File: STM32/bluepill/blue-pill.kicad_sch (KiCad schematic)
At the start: 35 parts

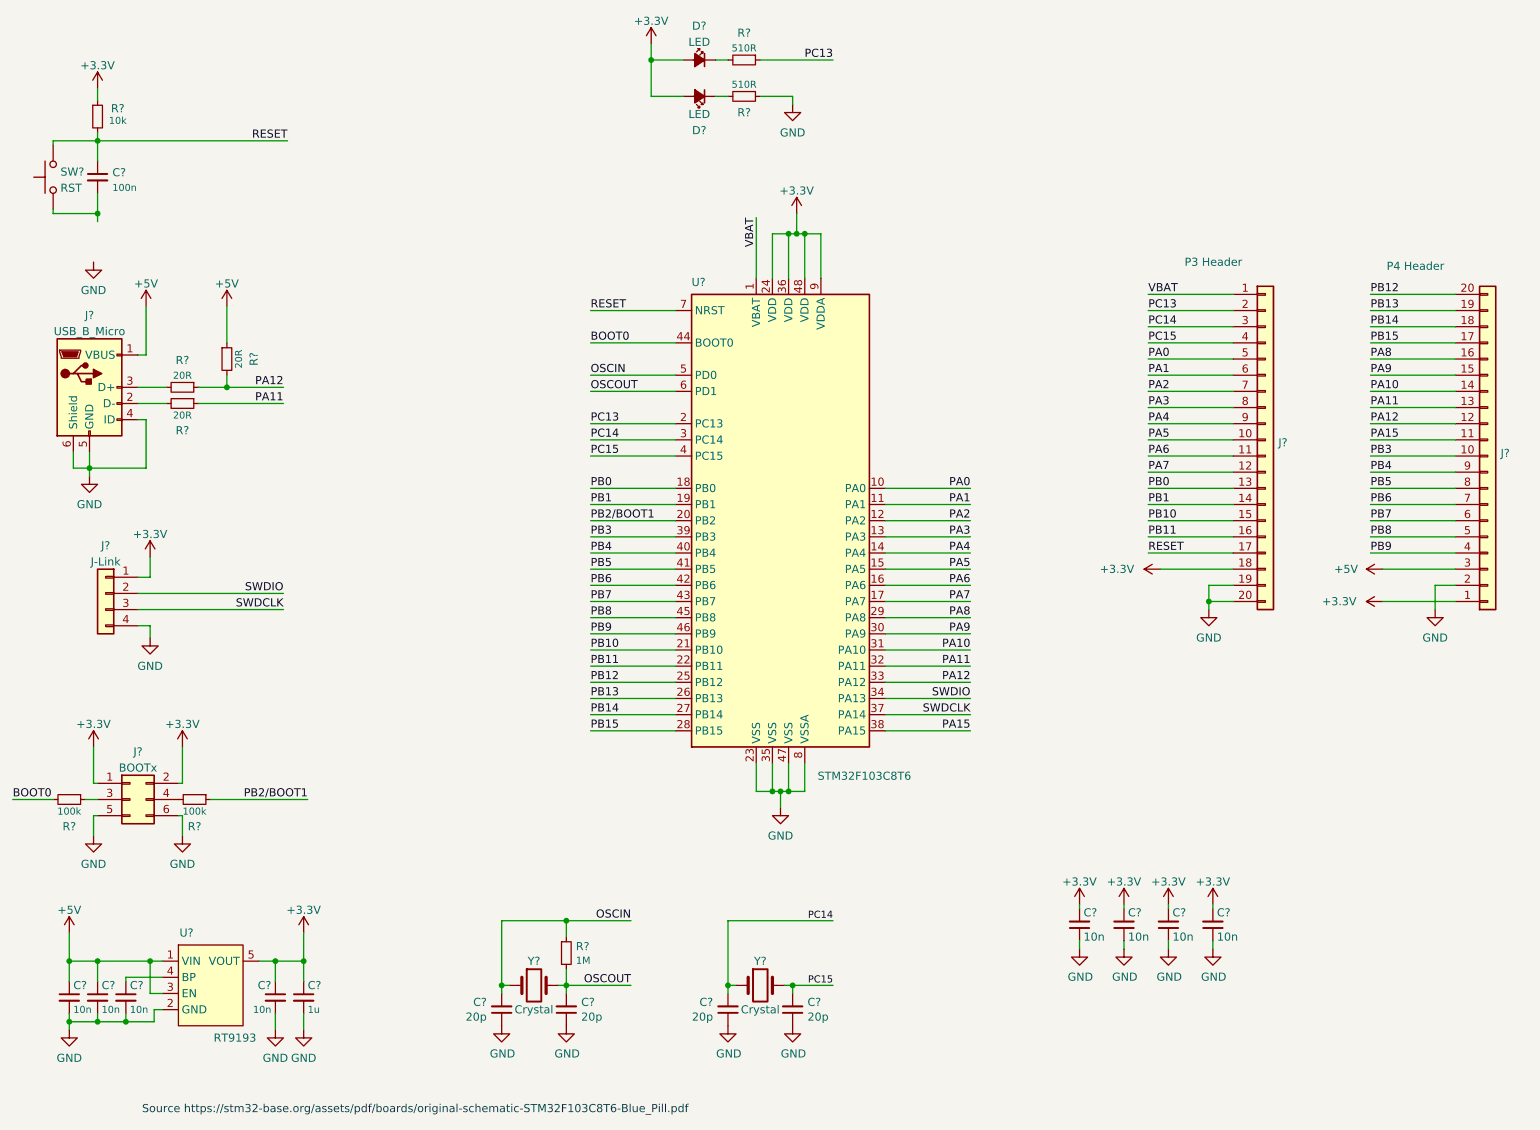
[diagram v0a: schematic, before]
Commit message: Fix ground on RST button
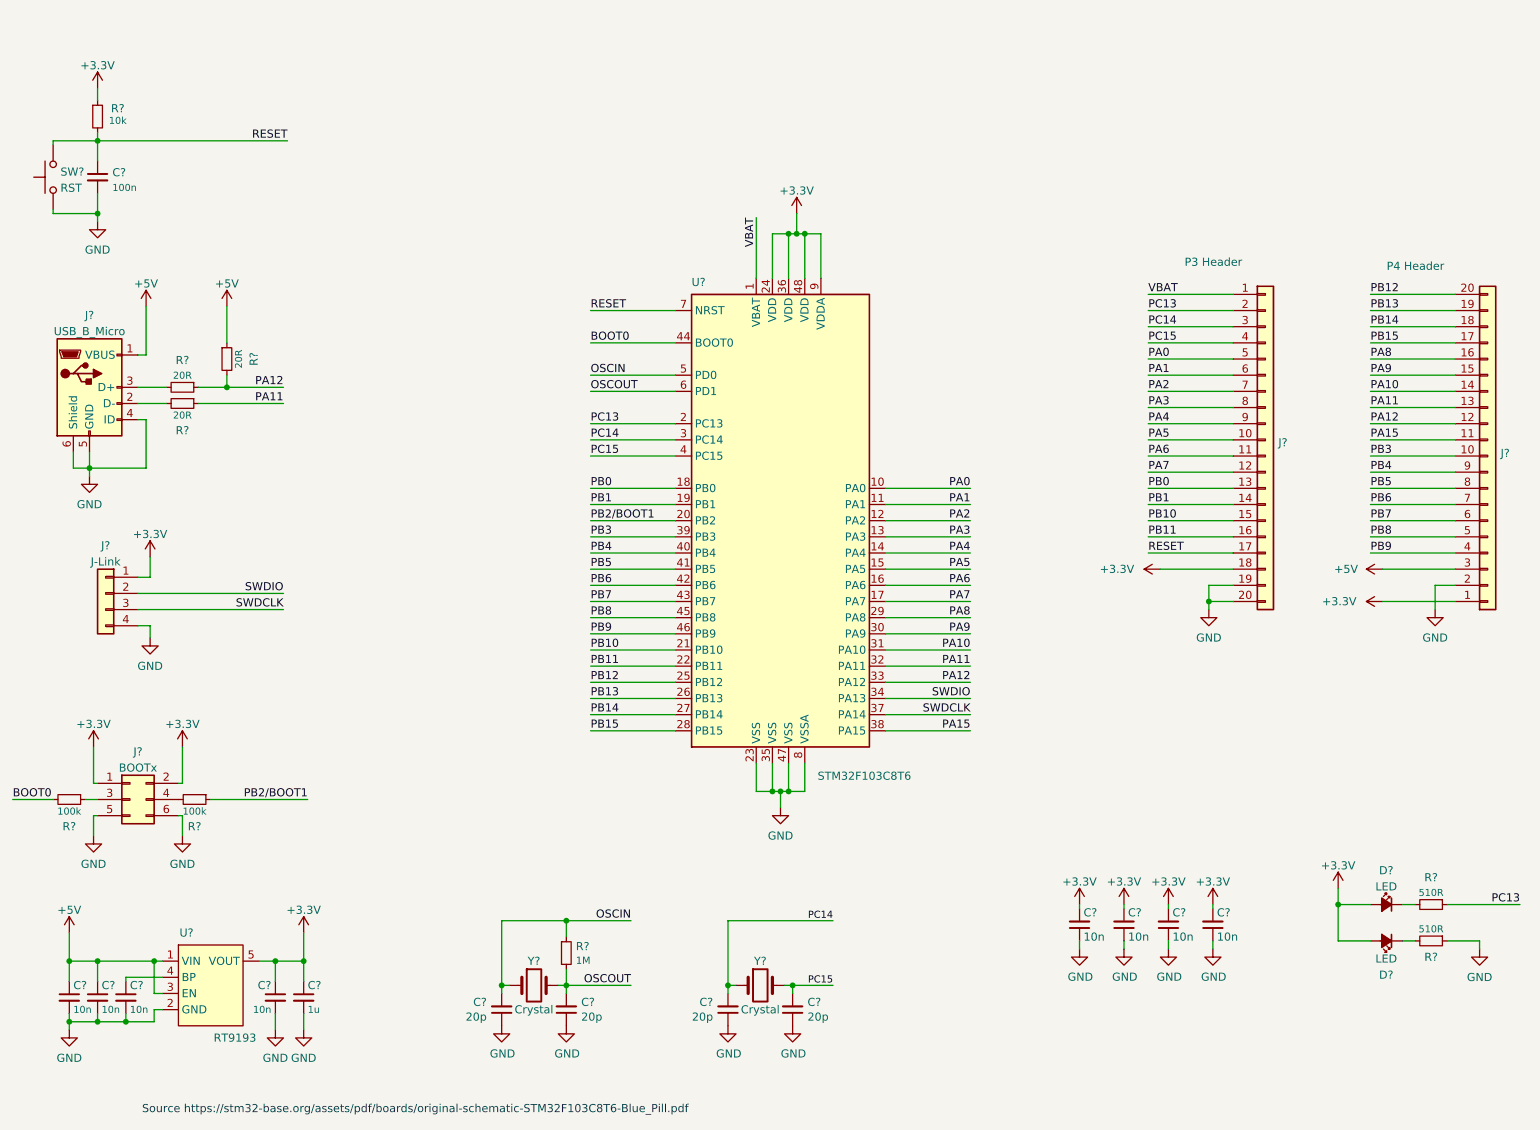
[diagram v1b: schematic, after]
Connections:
- net GND: now also C?.2, SW?.1
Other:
- moved on the sheet: D?, R?

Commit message: Fix input in RT919.3 Fix some resistors values.
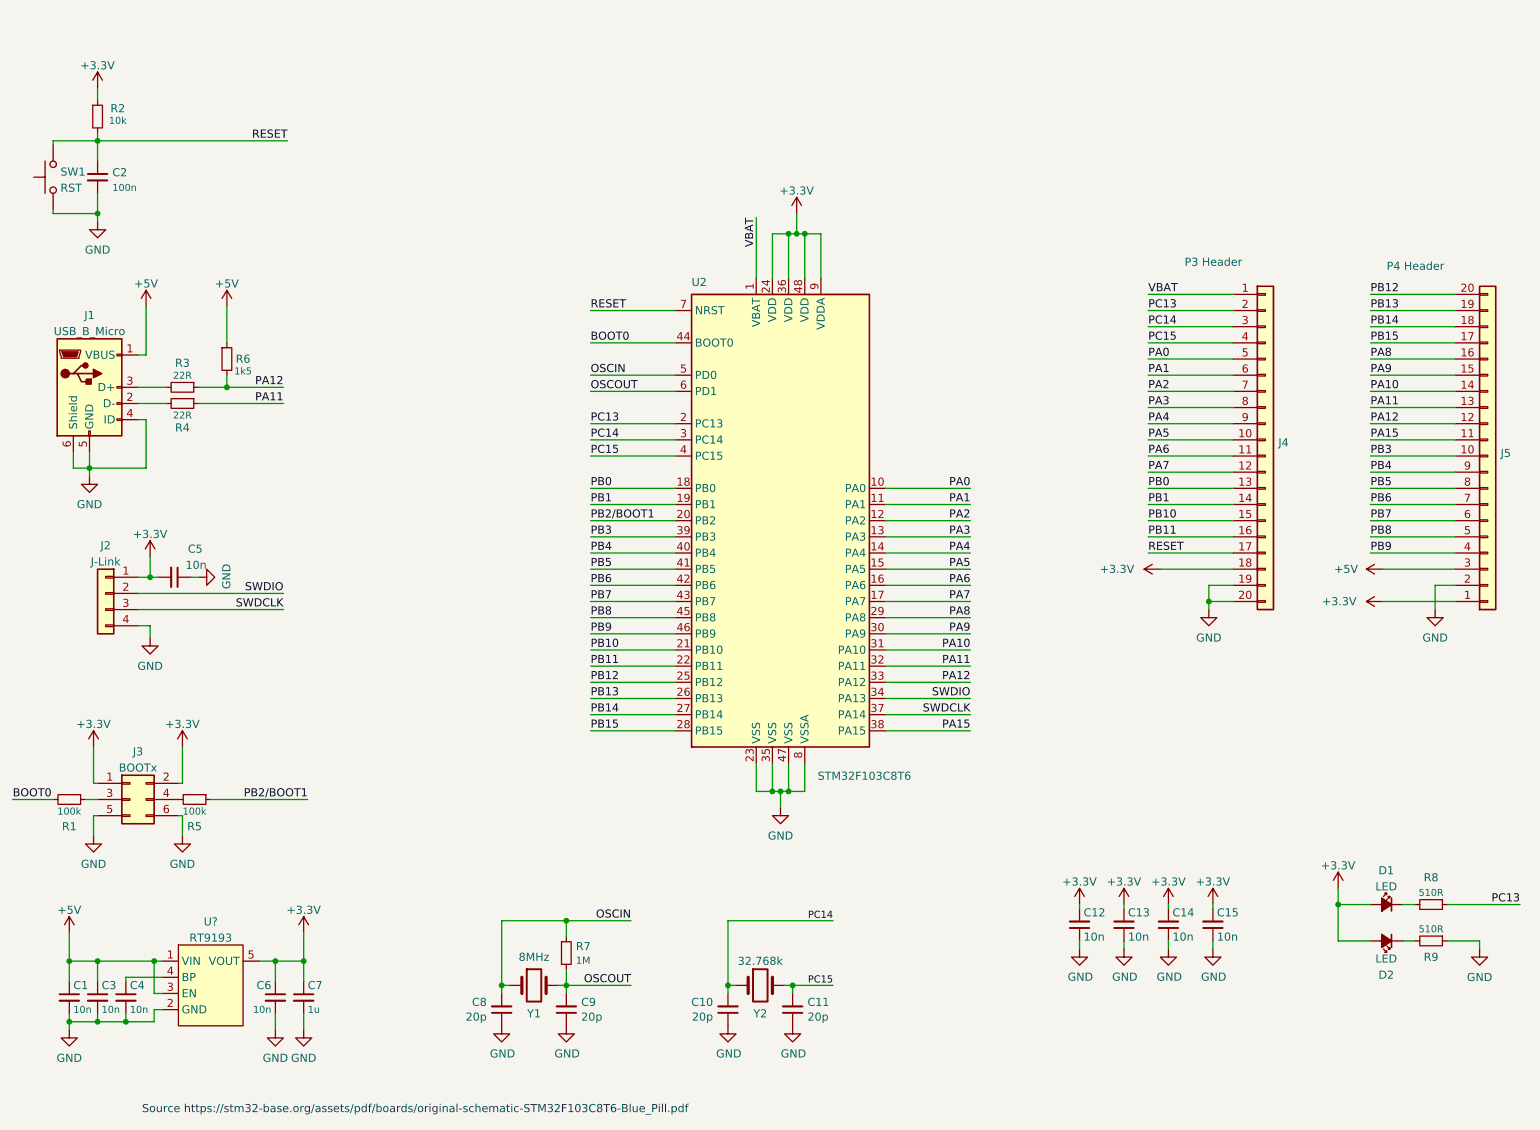
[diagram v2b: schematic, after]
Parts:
- removed U?: RT9193, symbol blue-pill:RT9193
- added C5: 10n, symbol Device:C_Small
- added U?: RT9193, symbol blue-pill:RT9193
- R3, R4: renamed from R?; value 20R -> 22R
- R6: renamed from R?; value 20R -> 1k5
- Y1: renamed from Y?; value Crystal -> 8MHz
- Y2: renamed from Y?; value Crystal -> 32.768k
- gave numbers to parts that had none: 29
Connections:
- net +3.3V: now also C5.2, U?.5 (VOUT)
- net +5V: now also U?.1 (VIN), U?.3 (EN)
- net GND: now also C5.1, U?.2 (GND)
- net at C4.1: now also U?.4 (BP)

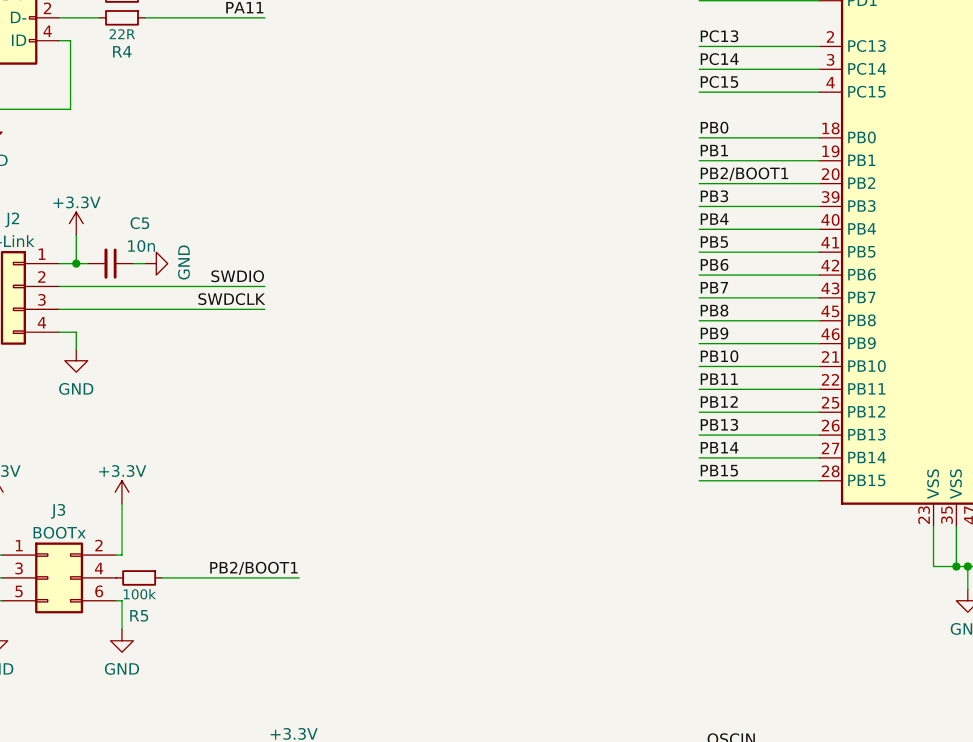
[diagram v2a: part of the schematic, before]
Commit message: Remove unused PB2 Ref.
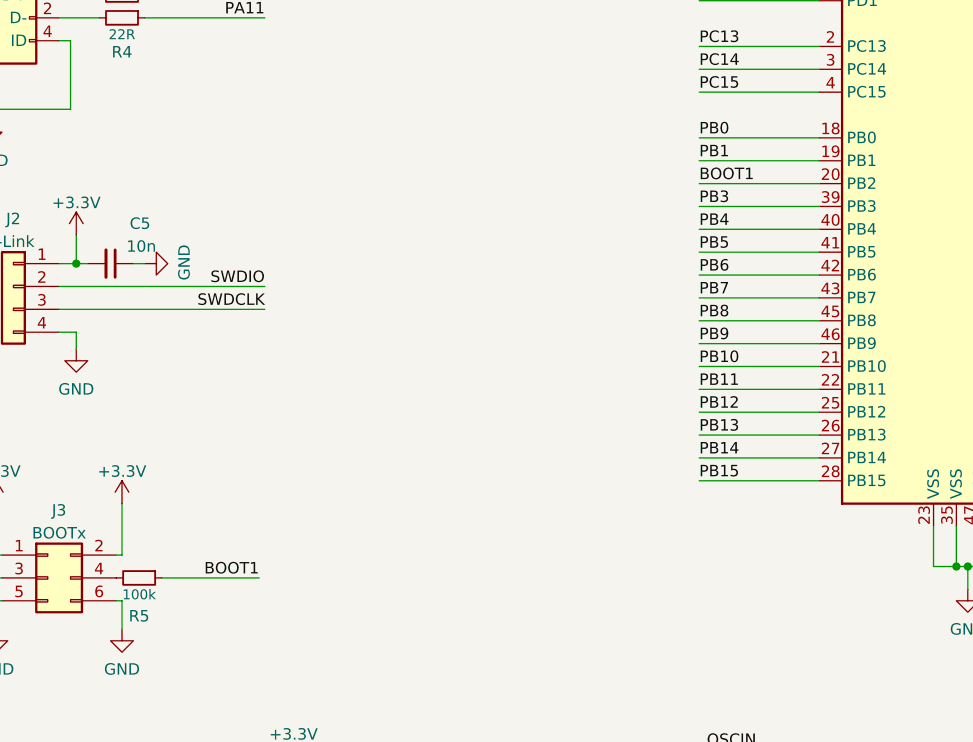
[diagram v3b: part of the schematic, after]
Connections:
- net PB2/BOOT1 renamed BOOT1
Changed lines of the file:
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@@
+    (stroke (width 0) (type default) (color 0 0 0 0))
+  )
+  (wire (pts (xy 62.23 142.24) (xy 73.025 142.24))
     (stroke (width 0) (type default) (color 0 0 0 0))
   )
@@
   )
   (wire (pts (xy 40.005 163.195) (xy 40.005 167.64))
-    (stroke (width 0) (type default) (color 0 0 0 0))
-  )
-  (wire (pts (xy 62.23 142.24) (xy 77.47 142.24))
     (stroke (width 0) (type default) (color 0 0 0 0))
   )
@@
     (effects (font (size 1.27 1.27)) (justify left bottom))
   )
-  (label "PB2{slash}BOOT1" (at 121.92 98.425 0)
+  (label "BOOT1" (at 121.92 98.425 0)
     (effects (font (size 1.27 1.27)) (justify left bottom))
   )
@@
     (effects (font (size 1.27 1.27)) (justify left bottom))
   )
-  (label "PB2{slash}BOOT1" (at 77.47 142.24 180)
-    (effects (font (size 1.27 1.27)) (justify right bottom))
-  )
+  (label "BOOT1" (at 73.025 142.24 180)
+    (effects (font (size 1.27 1.27)) (justify right bottom))
+  )

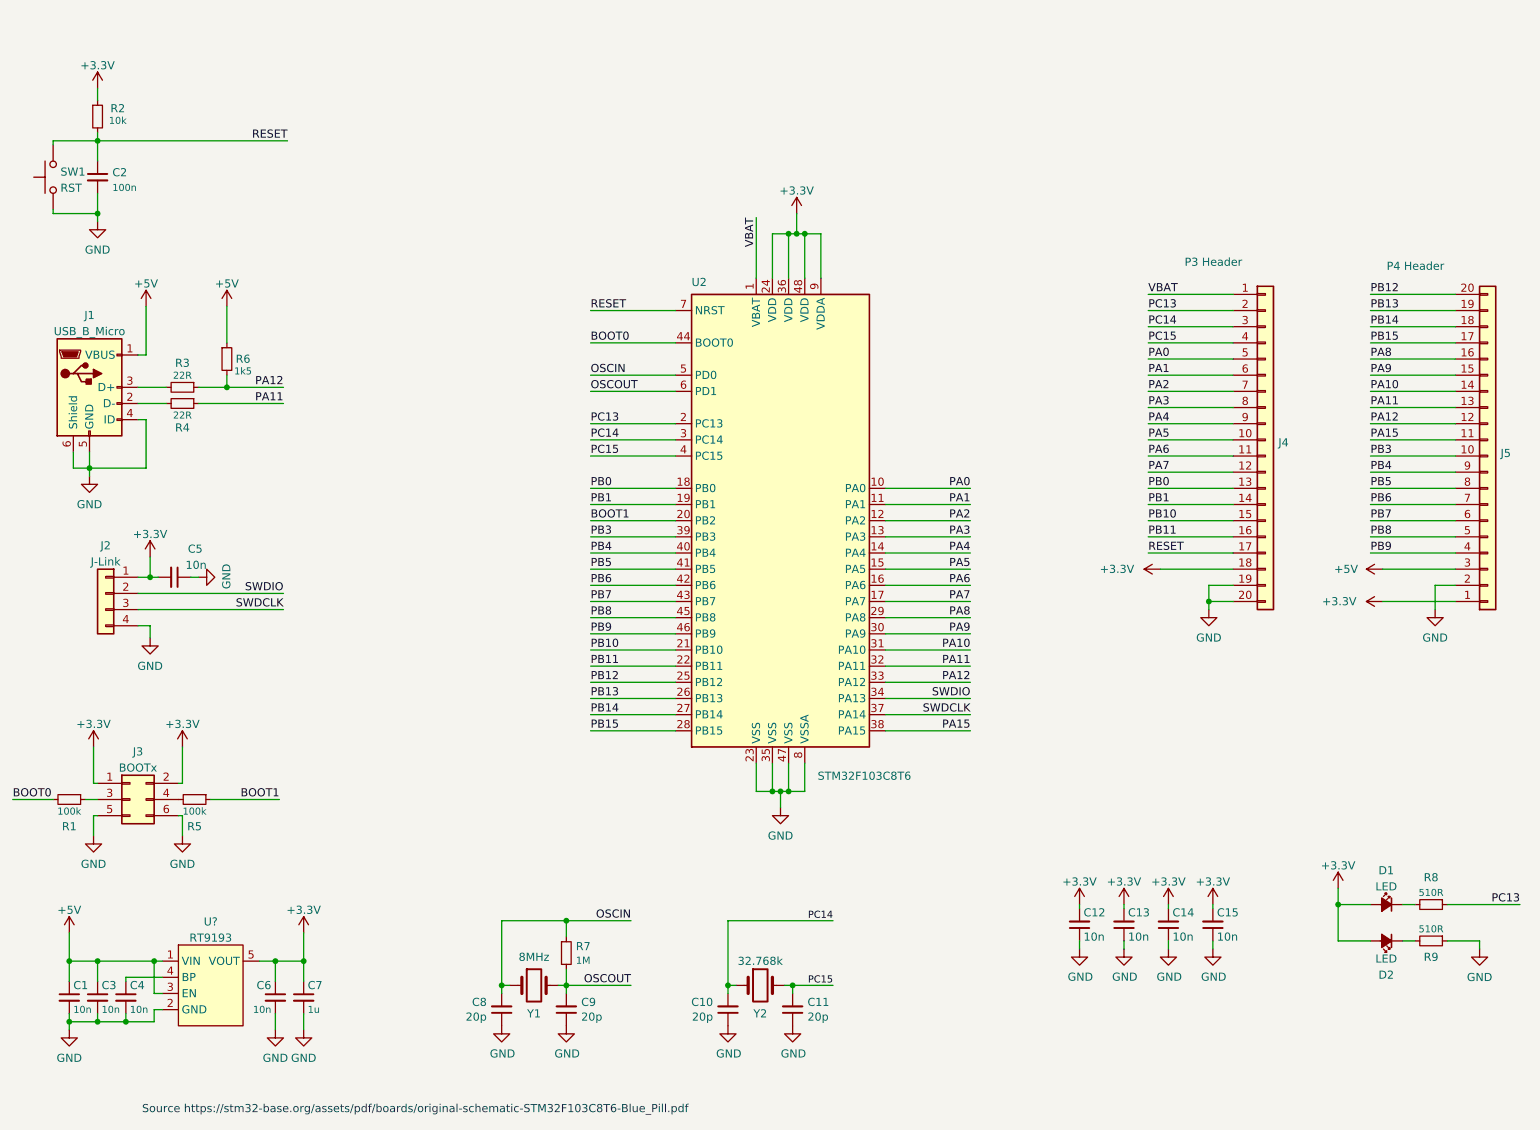
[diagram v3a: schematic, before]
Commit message: Fix annotation
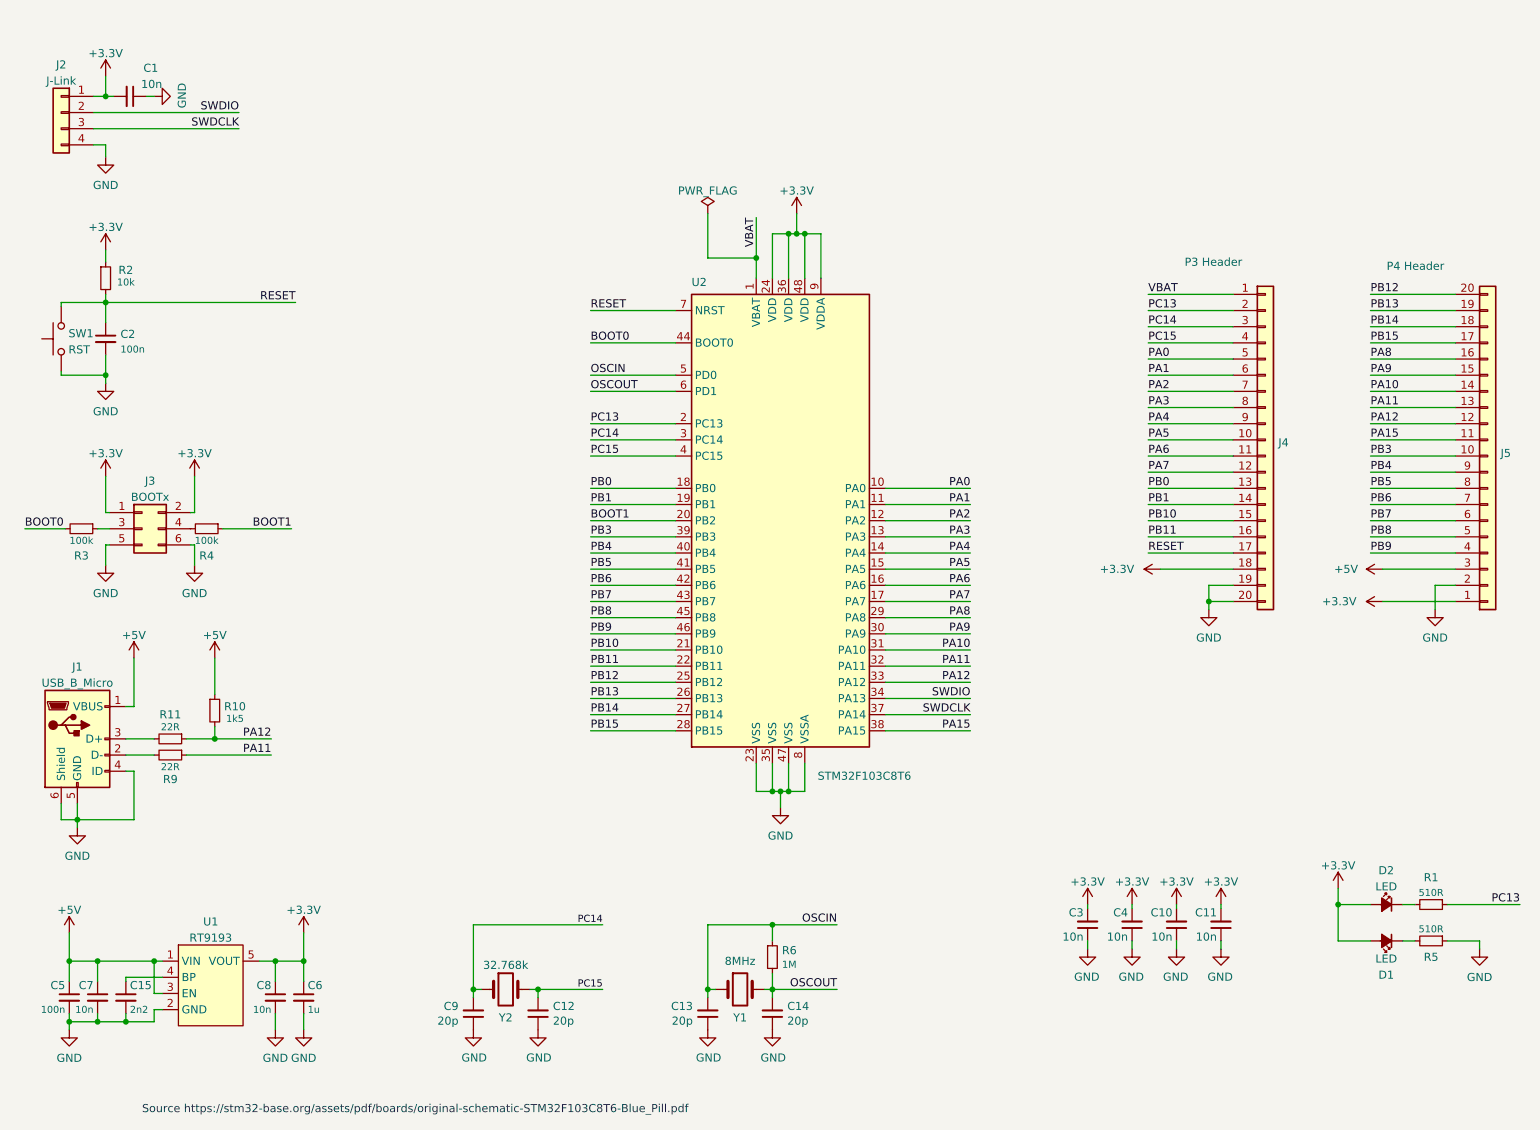
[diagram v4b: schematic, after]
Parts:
- C15: renamed from C4; value 10n -> 2n2
- C5: renamed from C1; value 10n -> 100n
- gave numbers to parts that had none: 1
- renumbered C5 to C1, C13 to C10, C12 to C11, C11 to C12, C8 to C13, C9 to C14, C15 to C3, C14 to C4, C7 to C6, C3 to C7, C6 to C8, C10 to C9, D2 to D1, D1 to D2, R8 to R1, R6 to R10, R3 to R11, R1 to R3, R5 to R4, R9 to R5, R7 to R6, R4 to R9
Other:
- moved on the sheet: C1, C10, C11, C12, C13, C14, C2, C3, C4, C9, J1, J2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
